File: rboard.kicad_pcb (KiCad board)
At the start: 2 copper layers, 249.9 x 149.9 mm, 377 parts, among them P1 Header 01x03, P10 Mini-Fit_2W, P11 Mini-Fit_2W, P12 Mini-Fit_2W, P13 Mini-Fit_2W, P14 Mini-Fit_6W, P15 Mini-Fit_8W, P16 Mini-Fit_18W, P17 Header 01x10, P18 Header 01x10, P19 Header 01x10, P2 Header 01x03, P20 Header 01x10, P21 Header 01x10, P22 Header 01x10, P23 PCM, P24 Mini-Fit_10W, P25 Header 01x10, P3 RaspberryPi, P5 PSU 12V5V, P6 XFormer, P7 Interlock SW, P8 Mini-Fit_2W, P9 Mini-Fit_2W, Q1 IRL540, Q10 IRL540, Q11 IRL540, Q12 IRL540, Q13 IRL540, Q14 IRL540, Q15 IRL540, Q16 IRL540, Q2 IRL540, Q3 IRL540, Q33 IRL540, Q34 IRL540, Q35 IRL540, Q36 IRL540, Q37 IRL540, Q38 IRL540, Q39 IRL540, Q4 IRL540, Q40 IRL540, Q5 IRL540, Q6 IRL540, Q7 IRL540, Q8 IRL540, Q9 IRL540, U1 74HCT00, U10 CD74HCT165E, U11 CD74HCT165E, U12 CD74HCT165E, U13 SN74HC595N, U14 ULN2803A, U15 ULN2803A, U16 ULN2803A, U17 SN74HC595N, U18 OKR-T/3-W12-C, U2 ATTINY85-20PU, U3 SN74HCT244N, U4 SN74HC595N, U5 SN74HC595N, U6 SN74HC595N, U7 SN74HC595N, U8 CD74HCT165E, U9 CD74HCT165E

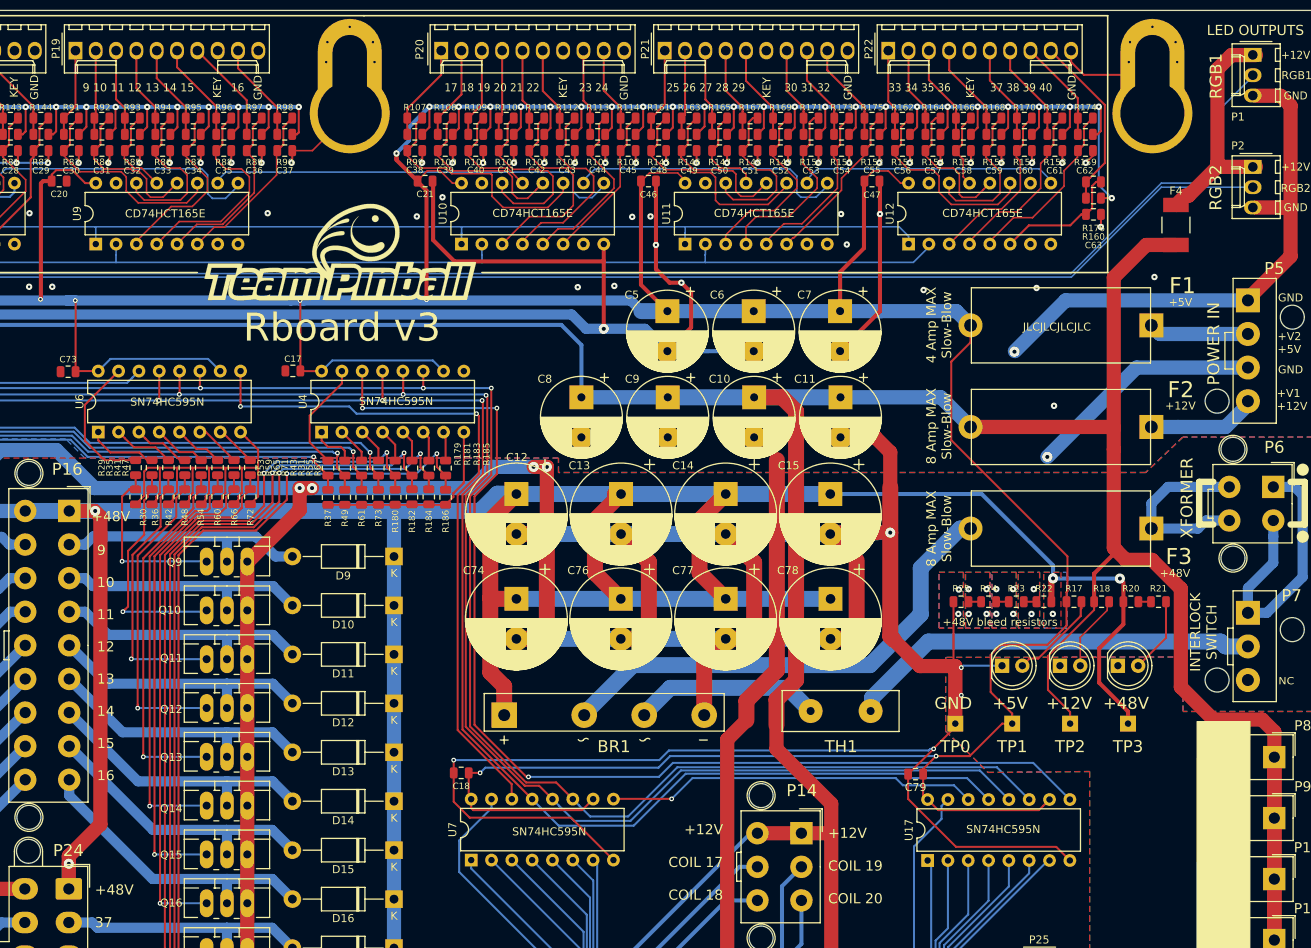
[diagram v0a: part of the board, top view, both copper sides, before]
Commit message: All 3D models added for 3d export
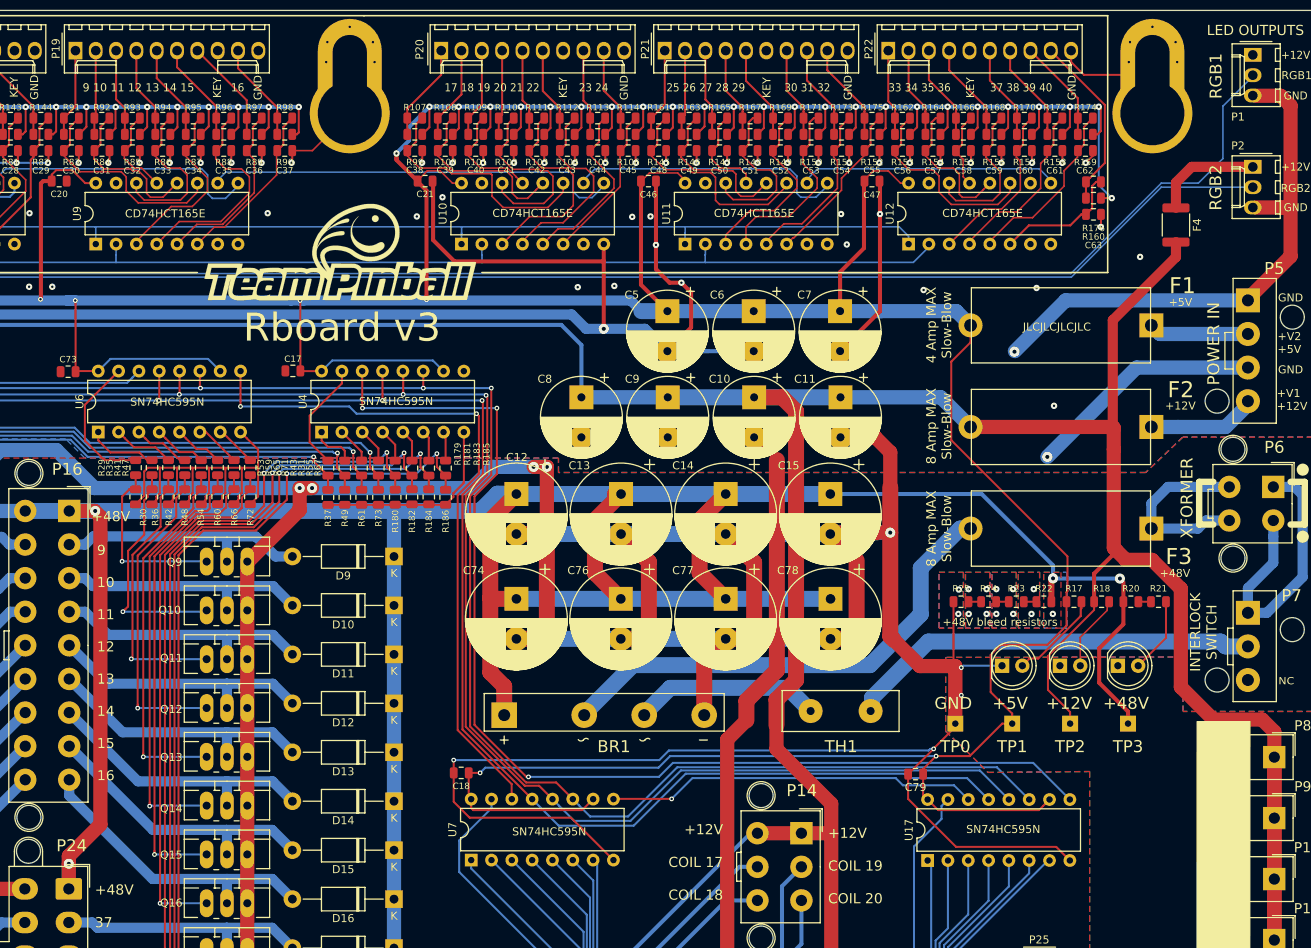
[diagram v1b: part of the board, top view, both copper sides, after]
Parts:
- F4: footprint lib:1812L125-16 -> lib:R_1812_4532Metric
- P24: value Mini-Fit_10W -> Molex_Mini-Fit_Jr_5566-10A2_2x05_P4.20mm_Vertical; footprint Connector_Molex:Molex_Mini-Fit_Jr_5566-10A2_2x05_P4.20mm_Vertical -> lib:Mini-Fit_10W
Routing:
- net +12V_LED: track 30.0 -> 13.6 mm
- net +12V: track 621.3 -> 619.5 mm
